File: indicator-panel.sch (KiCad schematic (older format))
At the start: 81 parts, among them J101 Power In, P101 Data in, P102 Data Out, P103 Power In, P104 Power Out, U101 MAX3094E, U102 STP16CP05, U103 STP16CP05, U104 MAX3033E, U106 STP16CP05, U108 LD1117S33CTR

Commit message: Make VDD and GND pins on chips visible.
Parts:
- R101, R102, R103: value 3.3kΩ -> 8.2kΩ
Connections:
- net labels removed: VCC, VDD
- wire segments 387 -> 304

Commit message: Added fiducials and ground pads
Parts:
- added J102, J103: GND, Mounting_Holes:MountingHole_3-5mm, symbol TEST_1P
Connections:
- net GND: now also J102.1, J103.1
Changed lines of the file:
@@
 	1    0    0    -1
 $EndComp
+$Comp
+L TEST_1P J103
+U 1 1 5A4009D2
+P 6650 8900
+F 0 "J103" H 6650 9170 50  0000 C CNN
+F 1 "GND" H 6650 9100 50  0000 C CNN
+F 2 "Mounting_Holes:MountingHole_3-5mm" H 6850 8900 50  0001 C CNN
+F 3 "" H 6850 8900 50  0001 C CNN
+	1    6650 8900
+	-1   0    0    1
+$EndComp
+$Comp
+L TEST_1P J102
+U 1 1 5A40116B
+P 6400 8900
+F 0 "J102" H 6400 9170 50  0000 C CNN
+F 1 "GND" H 6400 9100 50  0000 C CNN
+F 2 "Mounting_Holes:MountingHole_3-5mm" H 6600 8900 50  0001 C CNN
+F 3 "" H 6600 8900 50  0001 C CNN
+	1    6400 8900
+	-1   0    0    1
+$EndComp
+Wire Wire Line
+	6400 8900 6950 8900
+Connection ~ 6950 8900
+Connection ~ 6650 8900
 $EndSCHEMATC

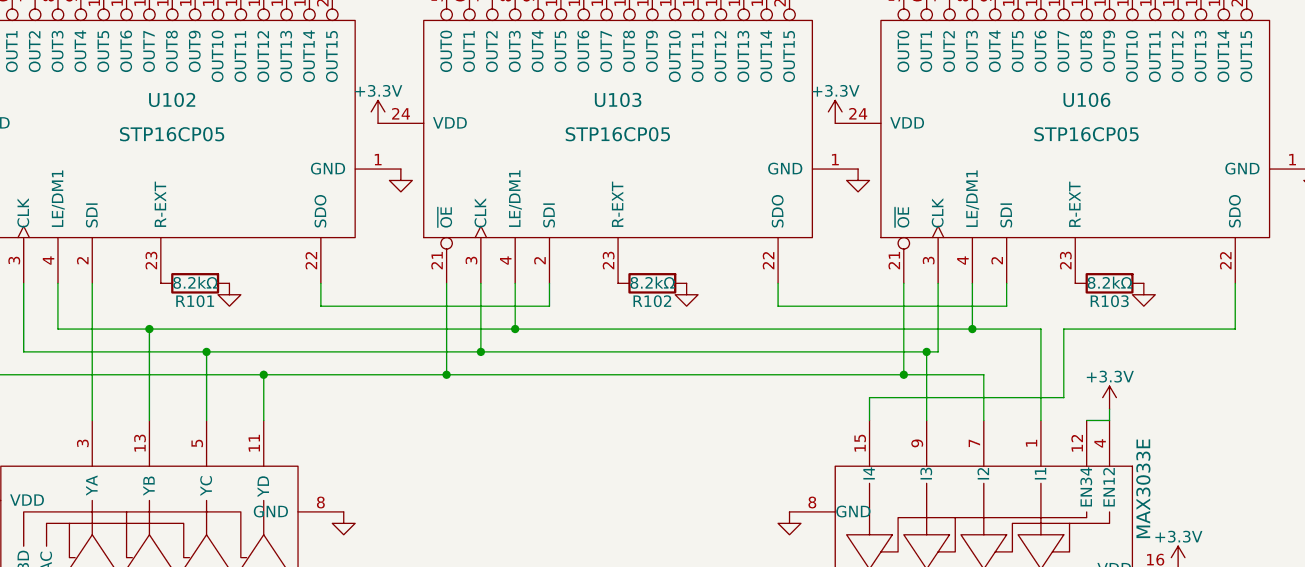
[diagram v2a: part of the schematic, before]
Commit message: Changed current limiting resistor to 8.2k
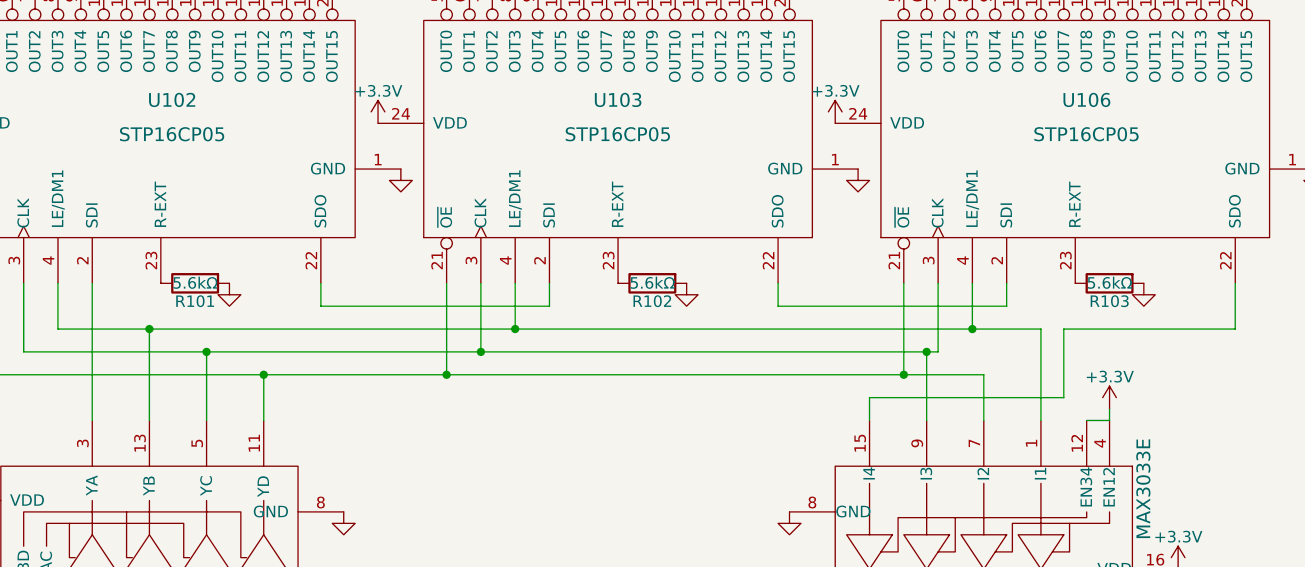
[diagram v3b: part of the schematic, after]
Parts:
- R101, R102, R103: value 8.2kΩ -> 5.6kΩ
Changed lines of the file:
@@
 P 2550 4800
 F 0 "R101" V 2630 4800 50  0000 C CNN
-F 1 "8.2kΩ" V 2550 4800 50  0000 C CNN
+F 1 "5.6kΩ" V 2550 4800 50  0000 C CNN
 F 2 "Resistors_SMD:R_0805" V 2480 4800 30  0001 C CNN
 F 3 "" H 2550 4800 30  0000 C CNN
@@
 P 4550 4800
 F 0 "R102" V 4630 4800 50  0000 C CNN
-F 1 "8.2kΩ" V 4550 4800 50  0000 C CNN
+F 1 "5.6kΩ" V 4550 4800 50  0000 C CNN
 F 2 "Resistors_SMD:R_0805" V 4480 4800 30  0001 C CNN
 F 3 "" H 4550 4800 30  0000 C CNN
@@
 P 6550 4800
 F 0 "R103" V 6630 4800 50  0000 C CNN
-F 1 "8.2kΩ" V 6550 4800 50  0000 C CNN
+F 1 "5.6kΩ" V 6550 4800 50  0000 C CNN
 F 2 "Resistors_SMD:R_0805" V 6480 4800 30  0001 C CNN
 F 3 "" H 6550 4800 30  0000 C CNN

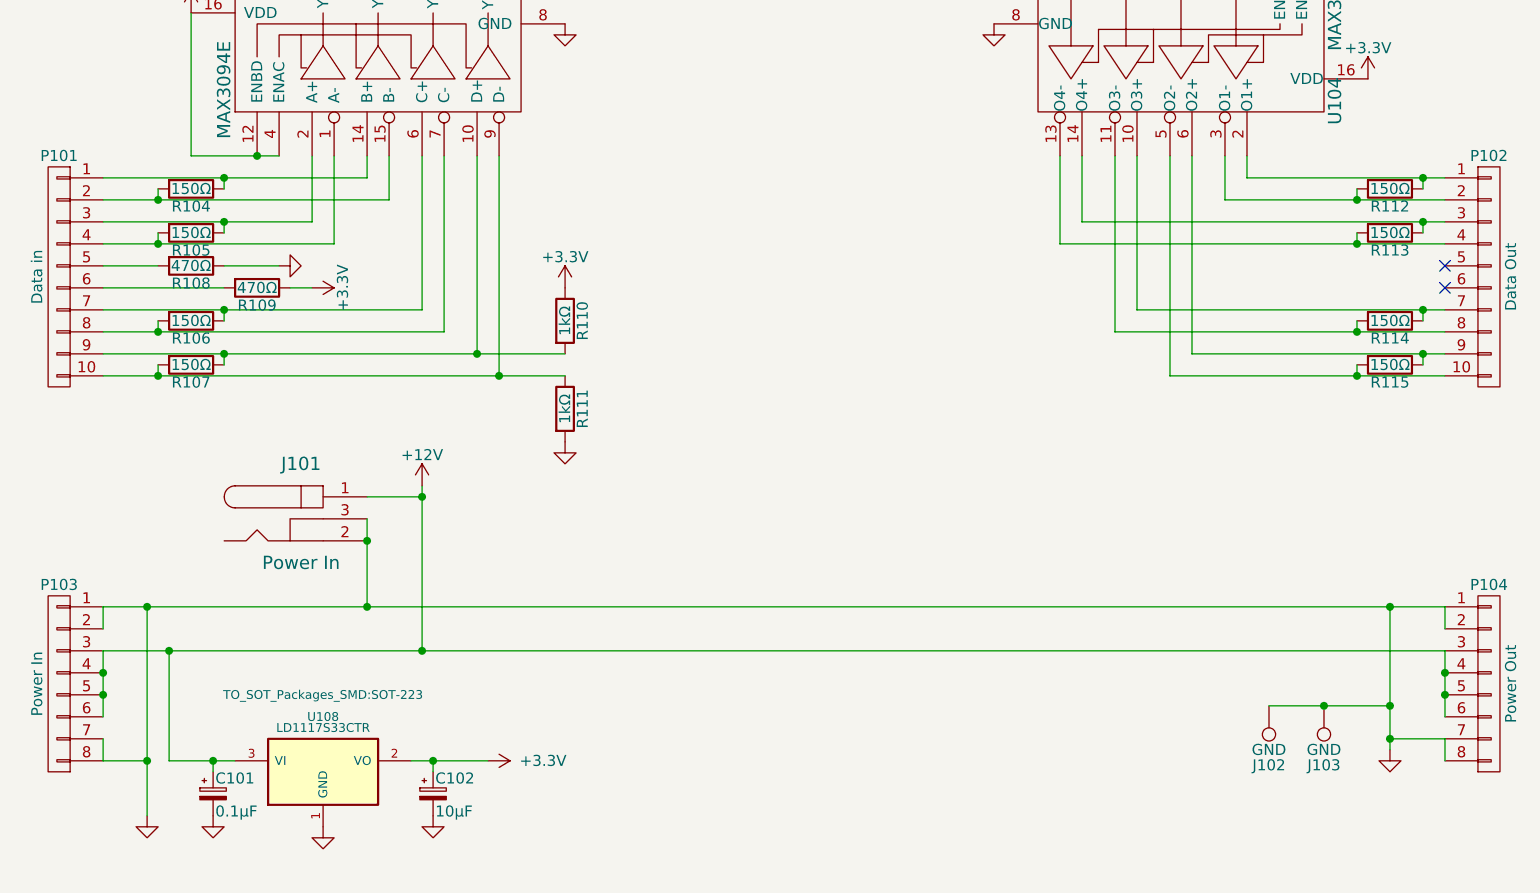
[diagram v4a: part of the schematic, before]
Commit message: Finalized v2 signal layout and submitted first batch for production.
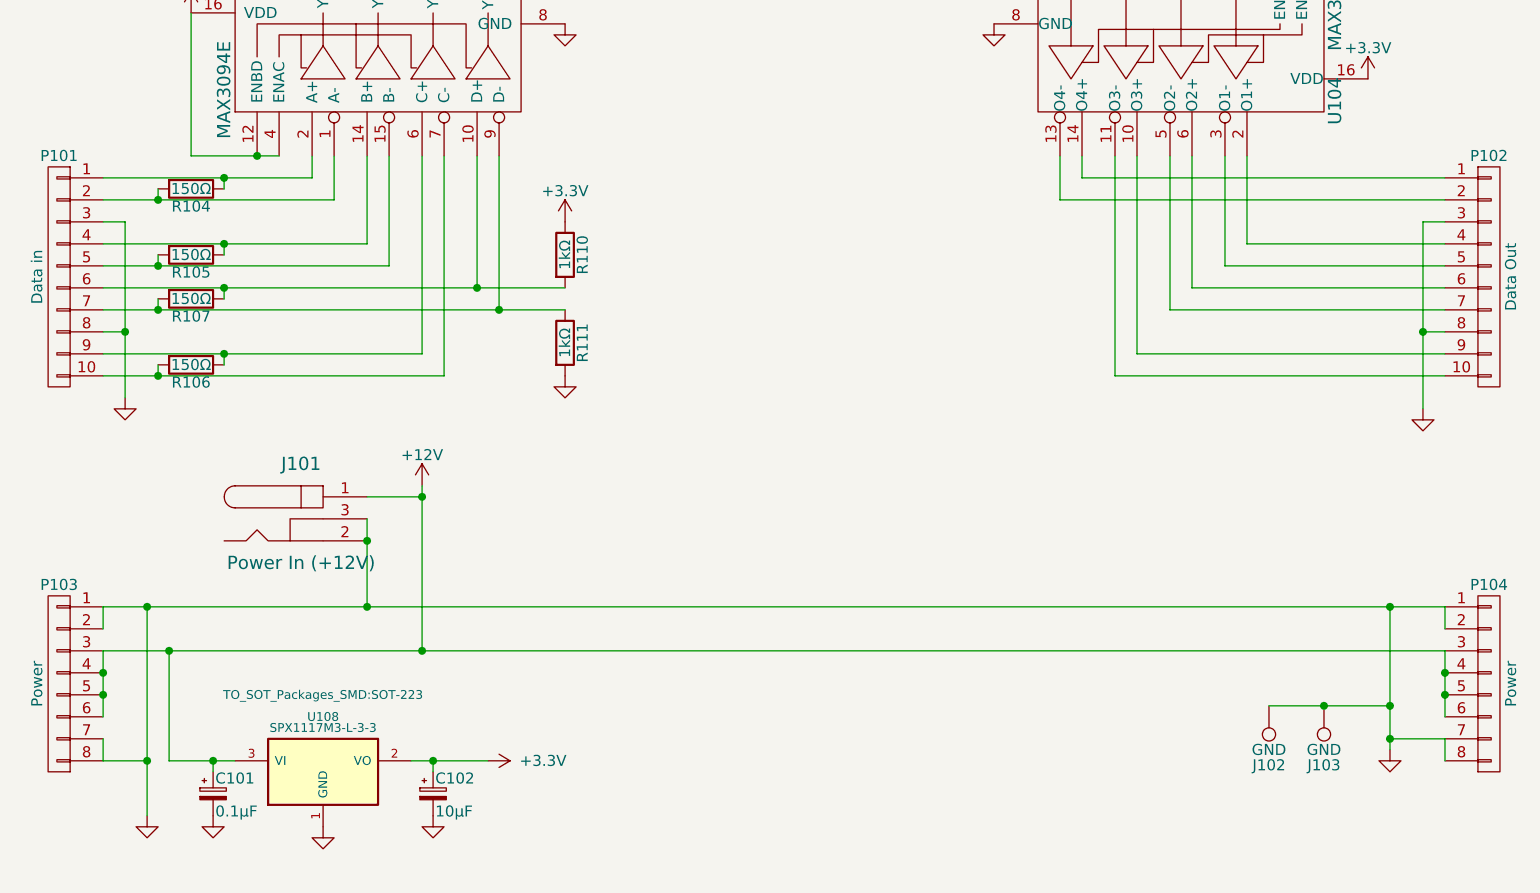
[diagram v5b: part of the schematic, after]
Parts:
- removed R108, R109: 470Ω, Resistors_SMD:R_0805, symbol R
- removed R112, R113, R114, R115: 150Ω, Resistors_SMD:R_0805, symbol R
- J101: value Power In -> Power In (+12V)
- P103: value Power In -> Power
- P104: value Power Out -> Power
- U108: value LD1117S33CTR -> SPX1117M3-L-3-3; manf# LD1117S33CTR -> SPX1117M3-L-3-3
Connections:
- net GND: now also P101.3 (P3), P101.8 (P8), P102.3 (P3), P102.8 (P8)
- net at R107.1, R110.2, U101.10 (D+): now also P101.6 (P6); no longer P101.9 (P9)
- net at P101.1 (P1), R104.1: now also U101.2 (A+); no longer U101.14 (B+)
- net at P101.2 (P2), R104.2: now also U101.1 (A-); no longer U101.15 (B-)
- net at R106.1, U101.6 (C+): now also P101.9 (P9); no longer P101.7 (P7)
- net at R106.2, U101.7 (C-): now also P101.10 (P10); no longer P101.8 (P8)
- net at R107.2, R111.1, U101.9 (D-): now also P101.7 (P7); no longer P101.10 (P10)
- net at P101.5 (P5): now also R105.2, U101.15 (B-)
- net at P102.1 (P1): now also U104.14 (O4+); no longer U104.2 (O1+)
- net at P102.10 (P10): now also U104.11 (O3-); no longer U104.5 (O2-)
- net at P102.2 (P2): now also U104.13 (O4-); no longer U104.3 (O1-)
- net at P102.4 (P4): now also U104.2 (O1+); no longer U104.13 (O4-)
- net at P102.5 (P5): now also U104.3 (O1-)
- net at P102.6 (P6): now also U104.6 (O2+)
- net at P102.7 (P7): now also U104.5 (O2-); no longer U104.10 (O3+)
- net at P102.9 (P9): now also U104.10 (O3+); no longer U104.6 (O2+)
- new net: P101.4 (P4), R105.1, U101.14 (B+)
- no-connect marks 2 -> 0
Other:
- moved on the sheet: R105, R106, R107, R110, R111

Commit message: Changed the tantalum capacitor footprint to more clearly show the positive end. Added some text around the power connector on the back.
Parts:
- C101: footprint Capacitors_Tantalum_SMD:TantalC_SizeR_EIA-2012 -> Capacitors_Tantalum_SMD:CP_Tantalum_Case-R_EIA-2012-12_Reflow
- C102: footprint Capacitors_Tantalum_SMD:TantalC_SizeR_EIA-2012 -> Capacitors_Tantalum_SMD:CP_Tantalum_Case-R_EIA-2012-12_Wave
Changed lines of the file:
@@
 F 0 "C101" H 1610 9370 50  0000 L CNN
 F 1 "0.1μF" H 1610 9220 50  0000 L CNN
-F 2 "Capacitors_Tantalum_SMD:TantalC_SizeR_EIA-2012" H 1600 9300 60  0001 C CNN
+F 2 "Capacitors_Tantalum_SMD:CP_Tantalum_Case-R_EIA-2012-12_Reflow" H 1600 9300 60  0001 C CNN
 F 3 "" H 1600 9300 60  0000 C CNN
 F 4 "TAJR104K020RNJ" H 1600 9300 60  0001 C CNN "manf#"
@@
 F 0 "C102" H 2610 9370 50  0000 L CNN
 F 1 "10μF" H 2610 9220 50  0000 L CNN
-F 2 "Capacitors_Tantalum_SMD:TantalC_SizeR_EIA-2012" H 2600 9300 60  0001 C CNN
+F 2 "Capacitors_Tantalum_SMD:CP_Tantalum_Case-R_EIA-2012-12_Wave" H 2600 9300 60  0001 C CNN
 F 3 "" H 2600 9300 60  0000 C CNN
 F 4 "TPSP106M010R2000" H 2600 9300 60  0001 C CNN "manf#"

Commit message: Update to KiCad 5.0
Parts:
- C101, C102: symbol CP_Small -> device:CP_Small
- C103, C104, C105, C106, C107: symbol C_Small -> device:C_Small
- D101, D102, D103, D104, D105, D106, D107, D108, D109, D110, D111, D112, D113, D114, D115, D116, D117, D118, D119, D120, D121, D122, D123, D124, D125, D126, D127, D128, D129, D130, D131, D132, D133, D134, D135, D136, D137, D138, D139, D140, D141, D142, D143, D144, D145, D146, D147, D148: symbol LED-45 -> myLib:LED-45
- J101: value Power In (+12V) -> Power In (5 - 12V); symbol BARREL_JACK -> conn:BARREL_JACK
- J102, J103: symbol TEST_1P -> indicator-panel-rescue:TEST_1P
- P101, P102: symbol CONN_01X10 -> conn:CONN_01X10
- P103, P104: symbol CONN_01X08 -> conn:CONN_01X08
- R101, R102, R103, R104, R105, R106, R107, R110, R111: symbol R -> device:R
- U101: symbol MAX3094E -> myLib:MAX3094E
- U102, U103, U106: symbol STP16CP05 -> myLib:STP16CP05
- U104: symbol MAX3033E -> myLib:MAX3033E
- U108: symbol LD1117S33CTR -> regul:LD1117S33CTR

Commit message: Bring in the cache and rescue files too.
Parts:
- C101, C102: symbol device:CP_Small -> indicator-panel-rescue:CP_Small-device
- C103, C104, C105, C106, C107: symbol device:C_Small -> indicator-panel-rescue:C_Small-device
- D101, D102, D103, D104, D105, D106, D107, D108, D109, D110, D111, D112, D113, D114, D115, D116, D117, D118, D119, D120, D121, D122, D123, D124, D125, D126, D127, D128, D129, D130, D131, D132, D133, D134, D135, D136, D137, D138, D139, D140, D141, D142, D143, D144, D145, D146, D147, D148: symbol myLib:LED-45 -> indicator-panel-rescue:LED-45-myLib
- J101: symbol conn:BARREL_JACK -> indicator-panel-rescue:BARREL_JACK-conn
- J102, J103: symbol indicator-panel-rescue:TEST_1P -> indicator-panel-rescue:TEST_1P-indicator-panel-rescue
- P101, P102: symbol conn:CONN_01X10 -> indicator-panel-rescue:CONN_01X10-conn
- P103, P104: symbol conn:CONN_01X08 -> indicator-panel-rescue:CONN_01X08-conn
- R101, R102, R103, R104, R105, R106, R107, R110, R111: symbol device:R -> indicator-panel-rescue:R-device
- U101: symbol myLib:MAX3094E -> indicator-panel-rescue:MAX3094E-myLib
- U102, U103, U106: symbol myLib:STP16CP05 -> indicator-panel-rescue:STP16CP05-myLib
- U104: symbol myLib:MAX3033E -> indicator-panel-rescue:MAX3033E-myLib
- U108: symbol regul:LD1117S33CTR -> indicator-panel-rescue:LD1117S33CTR-regul
